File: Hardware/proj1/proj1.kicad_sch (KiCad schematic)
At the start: 4 parts, among them SW1 SW_Push

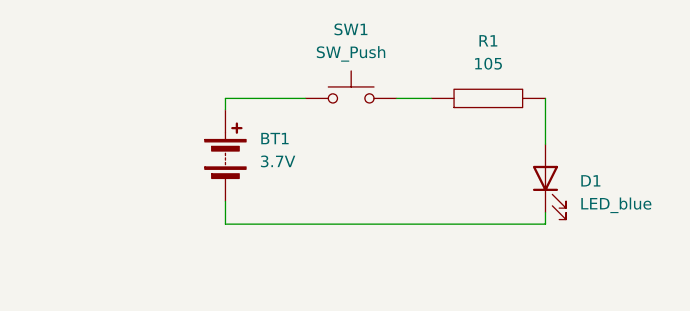
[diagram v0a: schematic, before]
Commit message: Finish Project 1 LED schematic and firmware
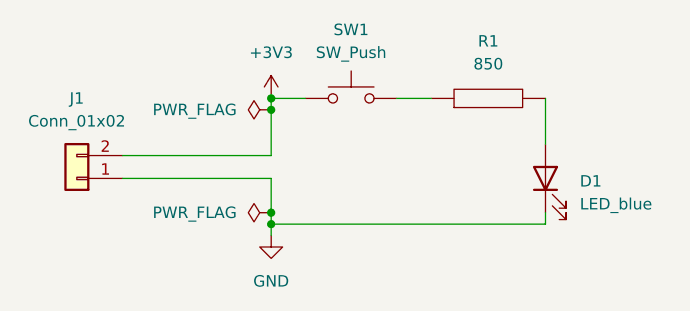
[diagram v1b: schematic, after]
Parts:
- removed BT1: 3.7V, symbol Device:Battery
- added J1: Conn_01x02, Connector_Molex:Molex_KK-254_AE-6410-02A_1x02_P2.54mm_Vertical, symbol Connector_Generic:Conn_01x02
- D1: footprint (none) -> layout:LED_0603_Symbol_on_F.SilkS; Notes (none) -> May change to blue
- R1: value 105 -> 850; footprint (none) -> Resistor_SMD:R_0603_1608Metric
- SW1: footprint (none) -> Button_Switch_SMD:SW_DIP_SPSTx01_Slide_6.7x4.1mm_W6.73mm_P2.54mm_LowProfile_JPin
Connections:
- net GND: now reaches D1.1 (K)
- net GND: now also J1.1 (Pin_1)
- net +3V3: now reaches SW1.1
- net +3V3: now also J1.2 (Pin_2)

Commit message: Add Project 1 PCB layout and DRC screenshots
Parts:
- SW1: footprint Button_Switch_SMD:SW_DIP_SPSTx01_Slide_6.7x4.1mm_W6.73mm_P2.54mm_LowProfile_JPin -> Button_Switch_SMD:SW_DIP_SPSTx01_Slide_6.7x4.1mm_W8.61mm_P2.54mm_LowProfile
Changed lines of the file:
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@@
 			)
 		)
-		(property "Footprint" "Button_Switch_SMD:SW_DIP_SPSTx01_Slide_6.7x4.1mm_W6.73mm_P2.54mm_LowProfile_JPin"
+		(property "Footprint" "Button_Switch_SMD:SW_DIP_SPSTx01_Slide_6.7x4.1mm_W8.61mm_P2.54mm_LowProfile"
 			(at 134.62 90.17 0)
 			(effects
